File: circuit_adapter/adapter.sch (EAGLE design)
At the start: 11 parts, among them CN1 5035521020, CN3 USB_BARE, X1 2510-

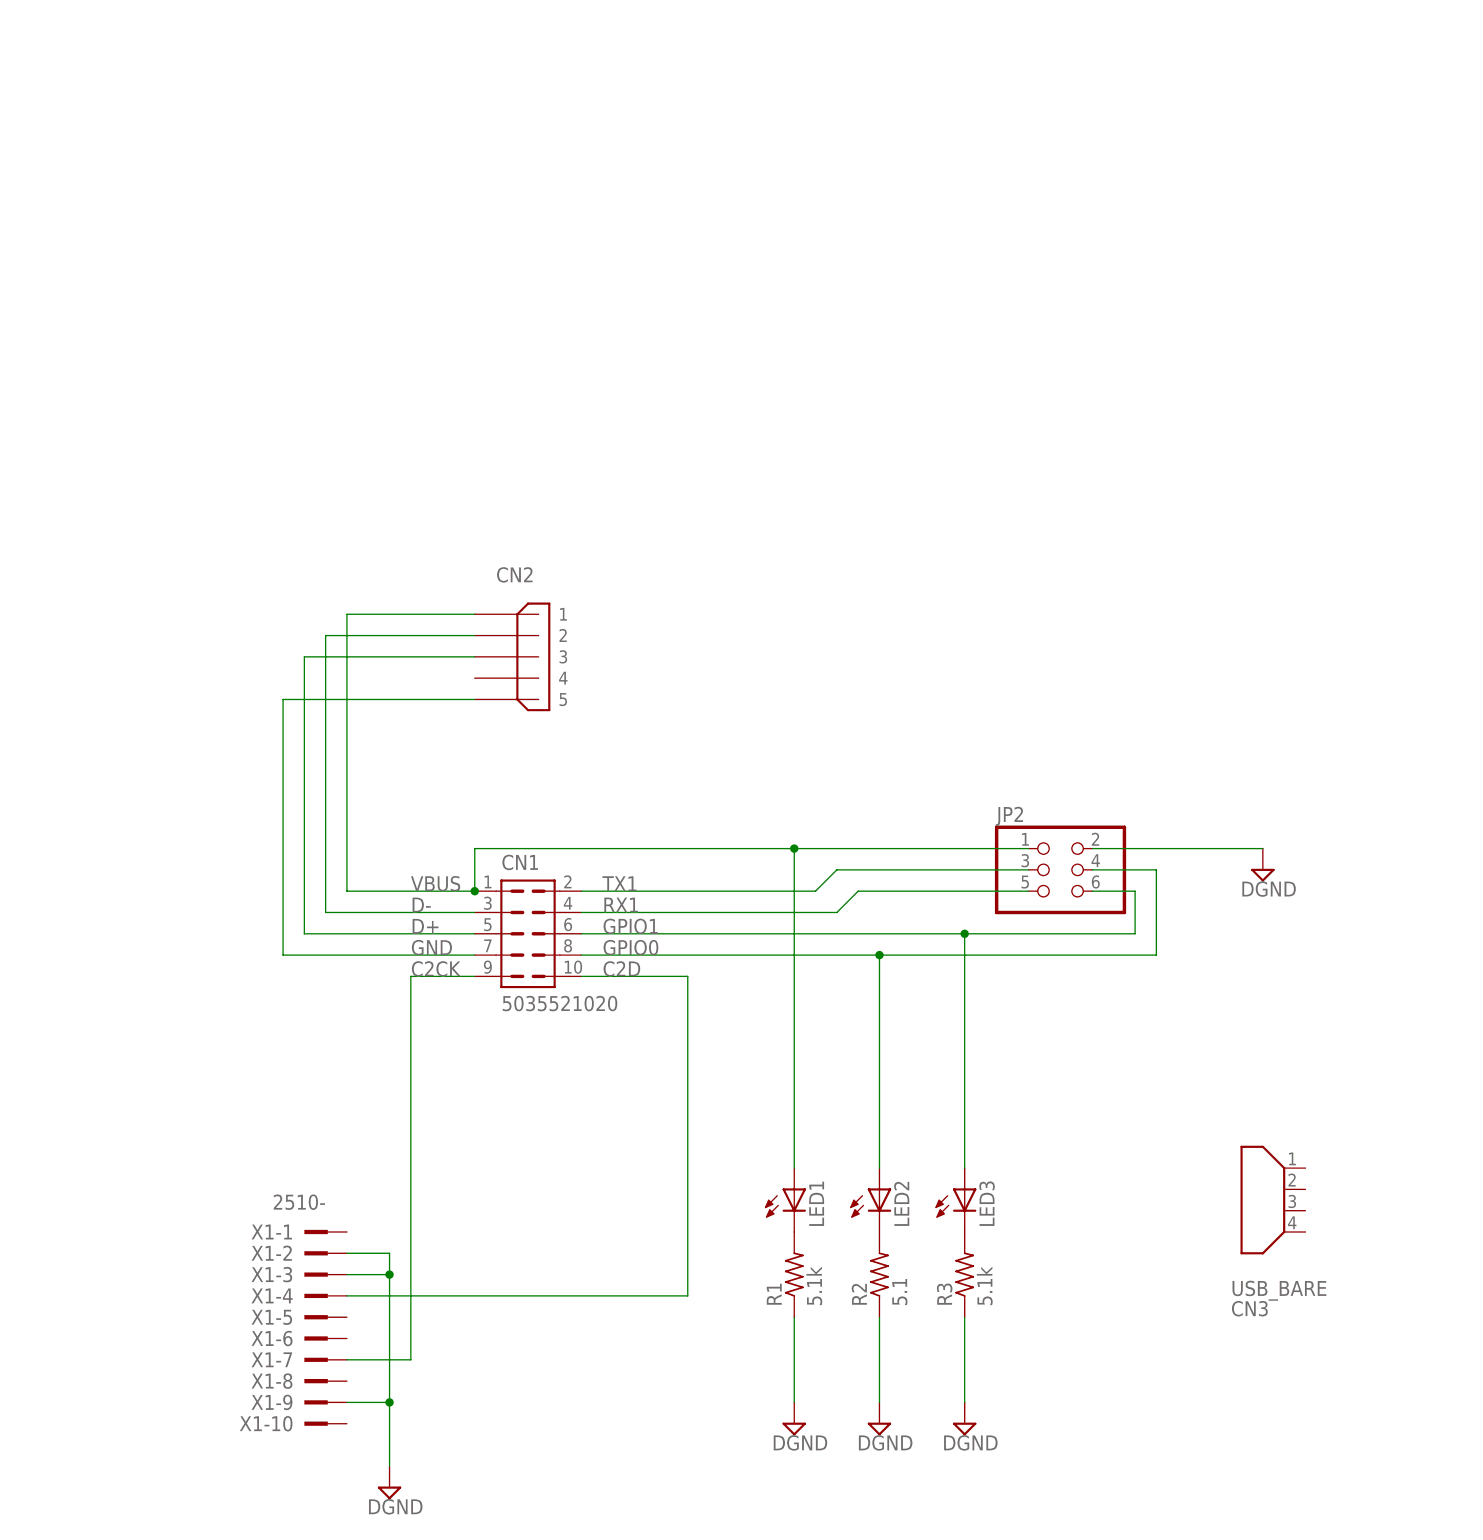
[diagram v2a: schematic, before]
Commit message: Modified adapter circuit
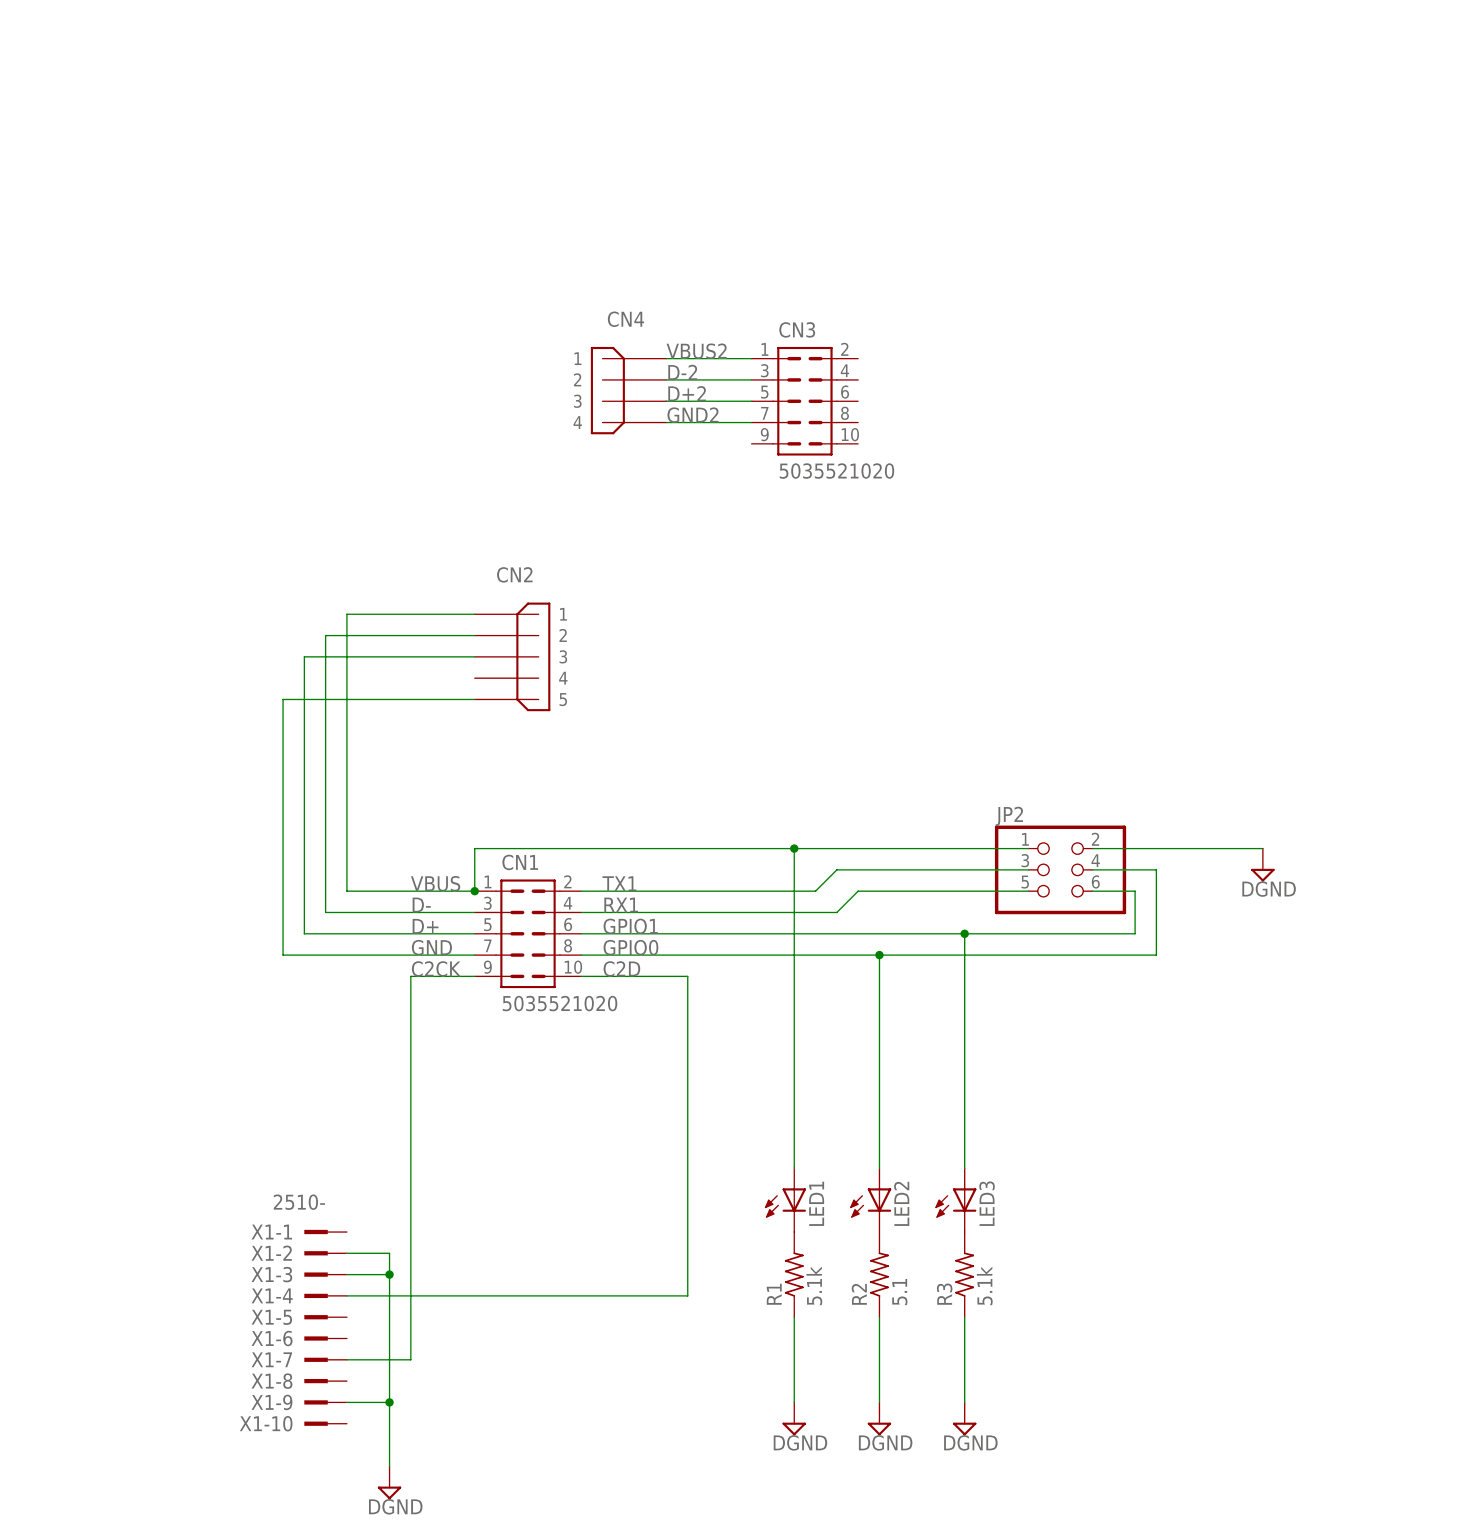
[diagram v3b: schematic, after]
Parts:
- added CN4: (no value), connector:USB
- CN3: value USB_BARE -> 5035521020; device connector:USB_BARE -> connector:5035521020
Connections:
- new net D+2: CN3.5, CN4.3
- new net D-2: CN3.3, CN4.2
- new net GND2: CN3.7, CN4.4
- new net VBUS2: CN3.1, CN4.1
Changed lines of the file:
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@@
 <part name="SUPPLY4" library="supply2" library_urn="urn:adsk.eagle:library:372" deviceset="DGND" device=""/>
 <part name="SUPPLY5" library="supply2" library_urn="urn:adsk.eagle:library:372" deviceset="DGND" device=""/>
-<part name="CN3" library="connector" deviceset="USB_BARE" device=""/>
+<part name="CN4" library="connector" deviceset="USB" device=""/>
+<part name="CN3" library="connector" deviceset="5035521020" device=""/>
 </parts>
 <sheets>
@@
 <attribute name="VALUE" x="91.313" y="-0.635" size="1.778" layer="96"/>
 </instance>
-<instance part="CN3" gate="G$1" x="132.08" y="27.94">
-<attribute name="NAME" x="125.73" y="15.367" size="1.778" layer="95"/>
-<attribute name="VALUE" x="125.73" y="17.78" size="1.778" layer="96"/>
+<instance part="CN4" gate="G$1" x="53.34" y="124.46" rot="MR0">
+<attribute name="NAME" x="55.88" y="133.35" size="1.778" layer="95" rot="MR0"/>
+<attribute name="VALUE" x="43.18" y="119.38" size="1.778" layer="96" rot="MR90"/>
+</instance>
+<instance part="CN3" gate="G$1" x="73.66" y="124.46">
+<attribute name="NAME" x="71.755" y="132.08" size="1.778" layer="95"/>
+<attribute name="VALUE" x="71.755" y="115.2525" size="1.778" layer="96"/>
 </instance>
 </instances>
@@
 </segment>
 </net>
+<net name="VBUS2" class="0">
+<segment>
+<pinref part="CN4" gate="G$1" pin="1"/>
+<pinref part="CN3" gate="G$1" pin="1"/>
+<wire x1="58.42" y1="129.54" x2="68.58" y2="129.54" width="0.1524" layer="91"/>
+<label x="58.42" y="129.54" size="1.778" layer="95"/>
+</segment>
+</net>
+<net name="D-2" class="1">
+<segment>
+<pinref part="CN4" gate="G$1" pin="2"/>
+<pinref part="CN3" gate="G$1" pin="3"/>
+<wire x1="58.42" y1="127" x2="68.58" y2="127" width="0.1524" layer="91"/>
+<label x="58.42" y="127" size="1.778" layer="95"/>
+</segment>
+</net>
+<net name="D+2" class="0">
+<segment>
+<pinref part="CN4" gate="G$1" pin="3"/>
+<pinref part="CN3" gate="G$1" pin="5"/>
+<wire x1="58.42" y1="124.46" x2="68.58" y2="124.46" width="0.1524" layer="91"/>
+<label x="58.42" y="124.46" size="1.778" layer="95"/>
+</segment>
+</net>
+<net name="GND2" class="0">
+<segment>
+<pinref part="CN4" gate="G$1" pin="4"/>
+<pinref part="CN3" gate="G$1" pin="7"/>
+<wire x1="58.42" y1="121.92" x2="68.58" y2="121.92" width="0.1524" layer="91"/>
+<label x="58.42" y="121.92" size="1.778" layer="95"/>
+</segment>
+</net>

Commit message: Modified adapter circuit and added garber zip
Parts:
- removed CN3: 5035521020, connector:5035521020
- removed CN4: (no value), connector:USB
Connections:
- removed net D+2: CN3.5, CN4.3
- removed net D-2: CN3.3, CN4.2
- removed net GND2: CN3.7, CN4.4
- removed net VBUS2: CN3.1, CN4.1
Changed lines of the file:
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@@
 <?xml version="1.0" encoding="utf-8"?>
 <!DOCTYPE eagle SYSTEM "eagle.dtd">
-<eagle version="9.1.3">
+<eagle version="9.2.0">
 <drawing>
 <settings>
@@
 <part name="SUPPLY4" library="supply2" library_urn="urn:adsk.eagle:library:372" deviceset="DGND" device=""/>
 <part name="SUPPLY5" library="supply2" library_urn="urn:adsk.eagle:library:372" deviceset="DGND" device=""/>
-<part name="CN4" library="connector" deviceset="USB" device=""/>
-<part name="CN3" library="connector" deviceset="5035521020" device=""/>
 </parts>
 <sheets>
@@
 <instance part="SUPPLY5" gate="G$1" x="93.98" y="2.54">
 <attribute name="VALUE" x="91.313" y="-0.635" size="1.778" layer="96"/>
-</instance>
-<instance part="CN4" gate="G$1" x="53.34" y="124.46" rot="MR0">
-<attribute name="NAME" x="55.88" y="133.35" size="1.778" layer="95" rot="MR0"/>
-<attribute name="VALUE" x="43.18" y="119.38" size="1.778" layer="96" rot="MR90"/>
-</instance>
-<instance part="CN3" gate="G$1" x="73.66" y="124.46">
-<attribute name="NAME" x="71.755" y="132.08" size="1.778" layer="95"/>
-<attribute name="VALUE" x="71.755" y="115.2525" size="1.778" layer="96"/>
 </instance>
 </instances>
@@
 </segment>
 </net>
-<net name="VBUS2" class="0">
-<segment>
-<pinref part="CN4" gate="G$1" pin="1"/>
-<pinref part="CN3" gate="G$1" pin="1"/>
-<wire x1="58.42" y1="129.54" x2="68.58" y2="129.54" width="0.1524" layer="91"/>
-<label x="58.42" y="129.54" size="1.778" layer="95"/>
-</segment>
-</net>
-<net name="D-2" class="1">
-<segment>
-<pinref part="CN4" gate="G$1" pin="2"/>
-<pinref part="CN3" gate="G$1" pin="3"/>
-<wire x1="58.42" y1="127" x2="68.58" y2="127" width="0.1524" layer="91"/>
-<label x="58.42" y="127" size="1.778" layer="95"/>
-</segment>
-</net>
-<net name="D+2" class="0">
-<segment>
-<pinref part="CN4" gate="G$1" pin="3"/>
-<pinref part="CN3" gate="G$1" pin="5"/>
-<wire x1="58.42" y1="124.46" x2="68.58" y2="124.46" width="0.1524" layer="91"/>
-<label x="58.42" y="124.46" size="1.778" layer="95"/>
-</segment>
-</net>
-<net name="GND2" class="0">
-<segment>
-<pinref part="CN4" gate="G$1" pin="4"/>
-<pinref part="CN3" gate="G$1" pin="7"/>
-<wire x1="58.42" y1="121.92" x2="68.58" y2="121.92" width="0.1524" layer="91"/>
-<label x="58.42" y="121.92" size="1.778" layer="95"/>
-</segment>
-</net>

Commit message: Modified parts values
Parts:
- R2: value 5.1 -> 5.1k
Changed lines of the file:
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@@
 <part name="LED3" library="led" library_urn="urn:adsk.eagle:library:259" deviceset="LED" device="SML0603" package3d_urn="urn:adsk.eagle:package:15832/1"/>
 <part name="R1" library="rcl" library_urn="urn:adsk.eagle:library:334" deviceset="R-US_" device="R0402" package3d_urn="urn:adsk.eagle:package:23547/2" value="5.1k"/>
-<part name="R2" library="rcl" library_urn="urn:adsk.eagle:library:334" deviceset="R-US_" device="R0402" package3d_urn="urn:adsk.eagle:package:23547/2" value="5.1"/>
+<part name="R2" library="rcl" library_urn="urn:adsk.eagle:library:334" deviceset="R-US_" device="R0402" package3d_urn="urn:adsk.eagle:package:23547/2" value="5.1k"/>
 <part name="R3" library="rcl" library_urn="urn:adsk.eagle:library:334" deviceset="R-US_" device="R0402" package3d_urn="urn:adsk.eagle:package:23547/2" value="5.1k"/>
 <part name="SUPPLY3" library="supply2" library_urn="urn:adsk.eagle:library:372" deviceset="DGND" device=""/>
